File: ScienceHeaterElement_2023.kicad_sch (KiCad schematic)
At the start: 10 parts, among them Q1 BUK7M6R3-40EX, U1 LMT85DCK

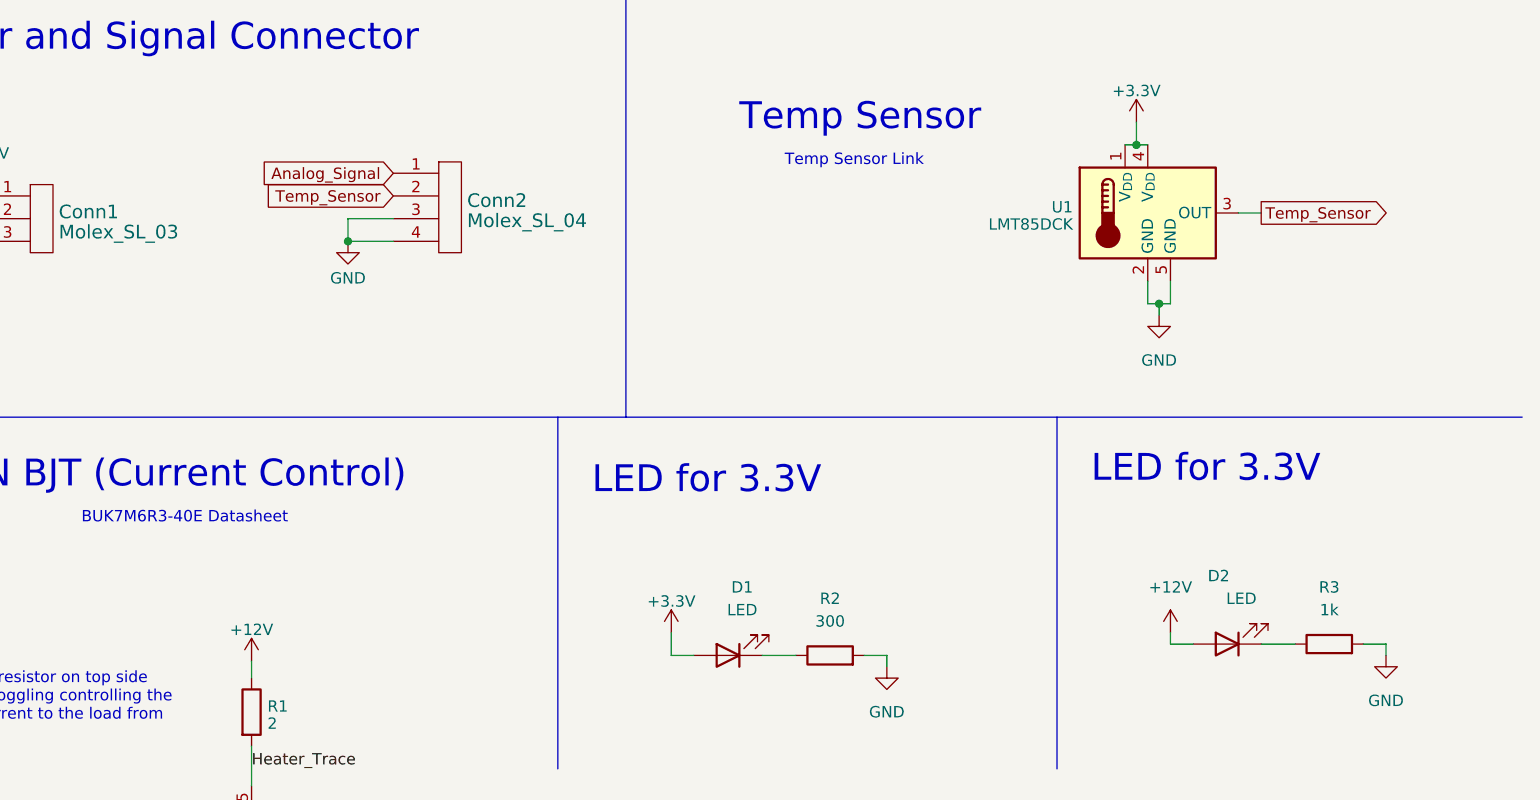
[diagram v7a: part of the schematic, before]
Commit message: Created PCB traces
Created PCB traces for Science Heater with components placed
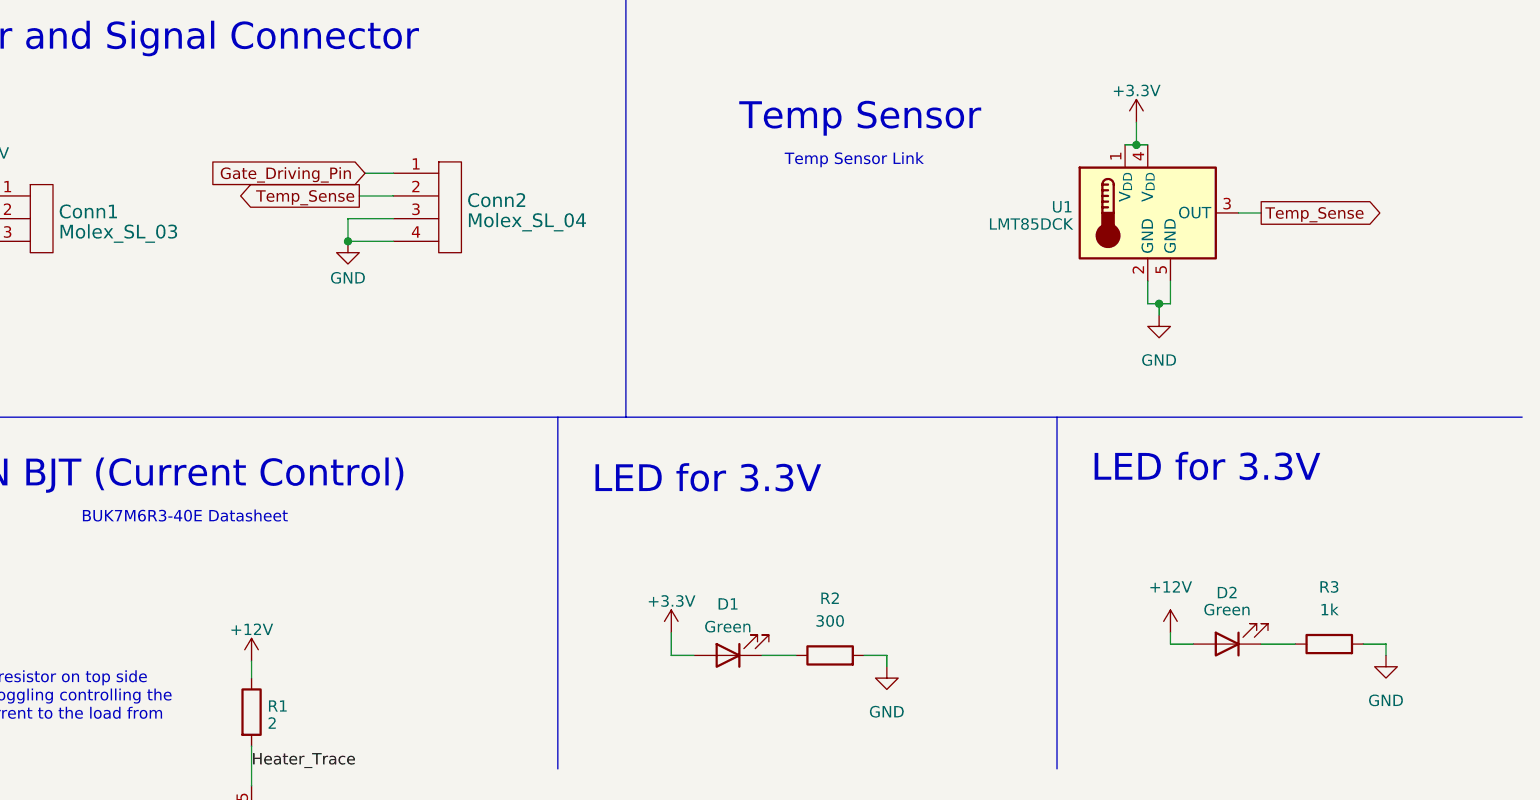
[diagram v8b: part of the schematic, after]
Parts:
- Conn1: footprint (none) -> MRDT_Connectors:MOLEX_SL_03_Horizontal
- Conn2: footprint (none) -> MRDT_Connectors:MOLEX_SL_04_Horizontal
- D1, D2: value LED -> Green; footprint (none) -> LED_SMD:LED_0603_1608Metric_Pad1.05x0.95mm_HandSolder
- R1, R2, R3, R4: footprint (none) -> Resistor_SMD:R_0603_1608Metric_Pad0.98x0.95mm_HandSolder
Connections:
- net Analog_Signal is gone; now on net Gate_Driving_Pin: Conn2.1
- net Temp_Sensor renamed Temp_Sense
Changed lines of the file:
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@@
+    (stroke (width 0) (type default))
+  )
+  (wire (pts (xy 68.58 37.465) (xy 71.755 37.465))
     (stroke (width 0) (type default))
   )
@@
   )
   (wire (pts (xy 156.21 49.53) (xy 156.21 52.07))
+    (stroke (width 0) (type default))
+  )
+  (wire (pts (xy 67.945 40.005) (xy 71.755 40.005))
     (stroke (width 0) (type default))
   )
@@
   (label "Heater_Trace" (at 55.88 104.14 0) (fields_autoplaced)
     (effects (font (size 1.27 1.27)) (justify left bottom))
-  )
-  (global_label "Analog_Signal" (shape input) (at 71.755 37.465 180) (fields_autoplaced)
-    (effects (font (size 1.27 1.27)) (justify right))
-    (property "Intersheetrefs" "${INTERSHEET_REFS}" (at 55.6053 37.465 0)
-      (effects (font (size 1.27 1.27)) (justify right) hide)
-    )
   )
   (global_label "Gate_Driving_Pin" (shape input) (at 34.925 111.125 180) (fields_autoplaced)
@@
     )
   )
-  (global_label "Temp_Sensor" (shape output) (at 168.91 41.91 0) (fields_autoplaced)
+  (global_label "Gate_Driving_Pin" (shape input) (at 68.58 37.465 180) (fields_autoplaced)
+    (effects (font (size 1.27 1.27)) (justify right))
+    (property "Intersheetrefs" "${INTERSHEET_REFS}" (at 49.9505 37.465 0)
+      (effects (font (size 1.27 1.27)) (justify right) hide)
+    )
+  )
+  (global_label "Temp_Sense" (shape output) (at 168.91 41.91 0) (fields_autoplaced)
     (effects (font (size 1.27 1.27)) (justify left))
-    (property "Intersheetrefs" "${INTERSHEET_REFS}" (at 184.1717 41.91 0)
+    (property "Intersheetrefs" "${INTERSHEET_REFS}" (at 183.2457 41.91 0)
       (effects (font (size 1.27 1.27)) (justify left) hide)
     )
   )
-  (global_label "Temp_Sensor" (shape input) (at 71.755 40.005 180) (fields_autoplaced)
+  (global_label "Temp_Sense" (shape output) (at 67.945 40.005 180) (fields_autoplaced)
     (effects (font (size 1.27 1.27)) (justify right))
-    (property "Intersheetrefs" "${INTERSHEET_REFS}" (at 56.5727 40.005 0)
+    (property "Intersheetrefs" "${INTERSHEET_REFS}" (at 53.6093 40.005 0)
       (effects (font (size 1.27 1.27)) (justify right) hide)
     )
   )
   (symbol (lib_id "Device:LED") (at 109.22 91.44 180) (unit 1)
-    (in_bom yes) (on_board yes) (dnp no) (fields_autoplaced)
-    (property "Reference" "D1" (at 110.8075 83.82 0)
-      (effects (font (size 1.27 1.27)))
-    )
-    (property "Value" "LED" (at 110.8075 86.36 0)
-      (effects (font (size 1.27 1.27)))
-    )
-    (property "Footprint" "" (at 109.22 91.44 0)
+    (in_bom yes) (on_board yes) (dnp no)
+    (property "Reference" "D1" (at 109.22 85.725 0)
+      (effects (font (size 1.27 1.27)))
+    )
+    (property "Value" "Green" (at 109.22 88.265 0)
+      (effects (font (size 1.27 1.27)))
+    )
+    (property "Footprint" "LED_SMD:LED_0603_1608Metric_Pad1.05x0.95mm_HandSolder" (at 109.22 91.44 0)
       (effects (font (size 1.27 1.27)) hide)
     )
@@
       (effects (font (size 1.27 1.27)))
     )
-    (property "Footprint" "" (at 120.65 93.218 90)
+    (property "Footprint" "Resistor_SMD:R_0603_1608Metric_Pad0.98x0.95mm_HandSolder" (at 120.65 93.218 90)
       (effects (font (size 1.27 1.27)) hide)
     )
@@
   (symbol (lib_id "Device:LED") (at 165.1 90.17 180) (unit 1)
     (in_bom yes) (on_board yes) (dnp no)
-    (property "Reference" "D2" (at 164.1475 82.55 0)
-      (effects (font (size 1.27 1.27)))
-    )
-    (property "Value" "LED" (at 166.6875 85.09 0)
-      (effects (font (size 1.27 1.27)))
-    )
-    (property "Footprint" "" (at 165.1 90.17 0)
+    (property "Reference" "D2" (at 165.1 84.455 0)
+      (effects (font (size 1.27 1.27)))
+    )
+    (property "Value" "Green" (at 165.1 86.36 0)
+      (effects (font (size 1.27 1.27)))
+    )
+    (property "Footprint" "LED_SMD:LED_0603_1608Metric_Pad1.05x0.95mm_HandSolder" (at 165.1 90.17 0)
       (effects (font (size 1.27 1.27)) hide)
     )
@@
       (effects (font (size 1.524 1.524)) (justify left))
     )
-    (property "Footprint" "" (at 76.835 46.355 0)
+    (property "Footprint" "MRDT_Connectors:MOLEX_SL_04_Horizontal" (at 76.835 46.355 0)
       (effects (font (size 1.524 1.524)) hide)
     )
@@
       (effects (font (size 1.27 1.27)) (justify left))
     )
-    (property "Footprint" "" (at 54.102 97.79 90)
+    (property "Footprint" "Resistor_SMD:R_0603_1608Metric_Pad0.98x0.95mm_HandSolder" (at 54.102 97.79 90)
       (effects (font (size 1.27 1.27)) hide)
     )
@@
       (effects (font (size 1.27 1.27)))
     )
-    (property "Footprint" "" (at 176.53 91.948 90)
+    (property "Footprint" "Resistor_SMD:R_0603_1608Metric_Pad0.98x0.95mm_HandSolder" (at 176.53 91.948 90)
       (effects (font (size 1.27 1.27)) hide)
     )
@@
       (effects (font (size 1.524 1.524)) (justify left))
     )
-    (property "Footprint" "" (at 31.115 46.355 0)
+    (property "Footprint" "MRDT_Connectors:MOLEX_SL_03_Horizontal" (at 31.115 46.355 0)
       (effects (font (size 1.524 1.524)) hide)
     )
@@
       (effects (font (size 1.27 1.27)) (justify left))
     )
-    (property "Footprint" "" (at 37.592 119.38 90)
-      (effects (font (size 1.27 1.27)) hide)
-    )
+    (property "Footprint" "Resistor_SMD:R_0603_1608Metric_Pad0.98x0.95mm_HandSolder" (at 37.592 119.38 90)
+      (effects (font (size 1.27 1.27)) hide)
+    )
